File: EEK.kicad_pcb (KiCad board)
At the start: 2 copper layers, 165 x 51.8 mm, 52 parts, among them J1 Screw_Terminal_01x02

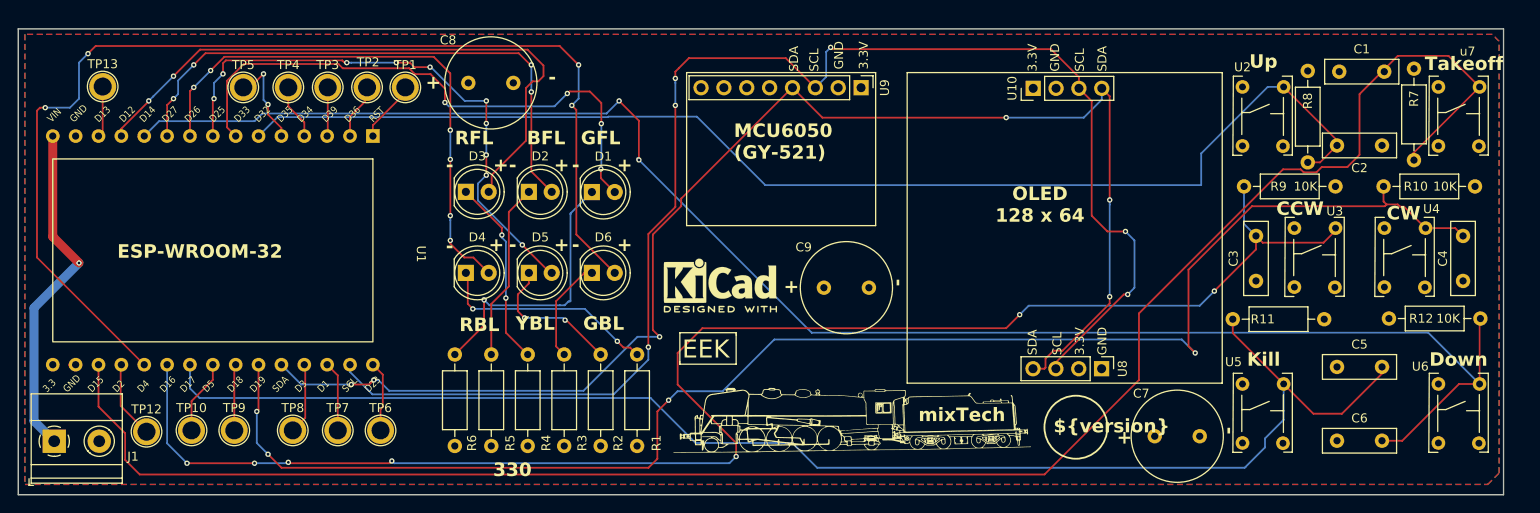
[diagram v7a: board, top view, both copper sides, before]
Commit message: Change footprint to SMD
Change footprint to SMD
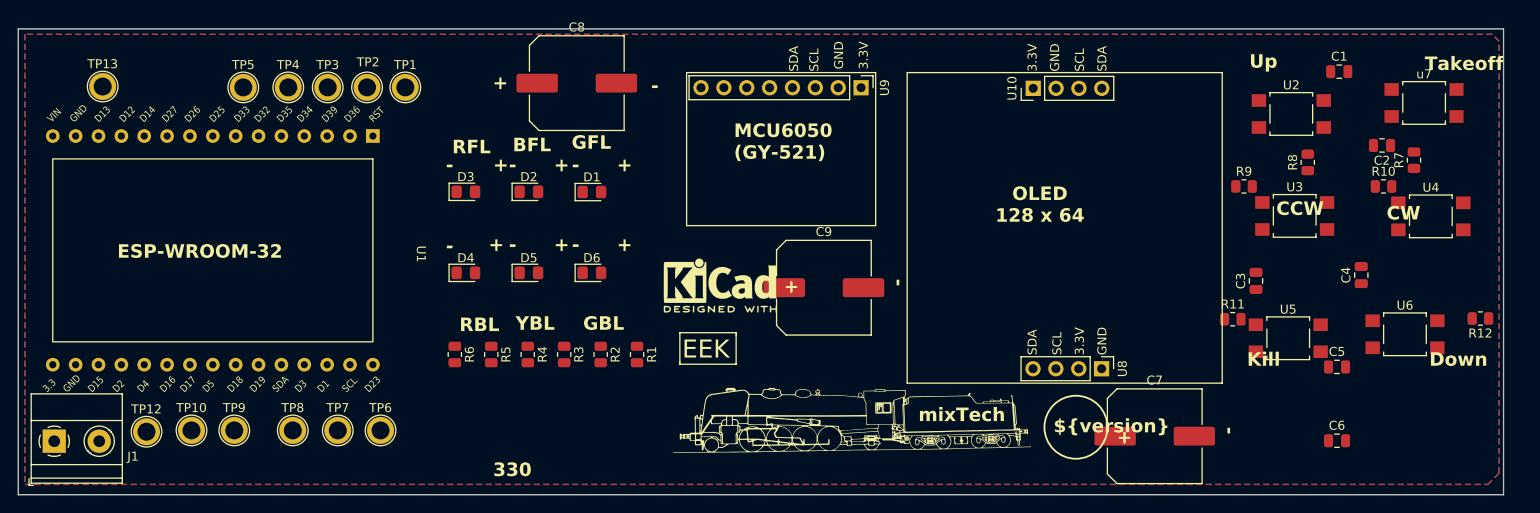
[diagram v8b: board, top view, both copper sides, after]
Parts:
- C1, C2, C3, C4, C5, C6: footprint Capacitor_THT:C_Disc_D8.0mm_W2.5mm_P5.00mm -> Capacitor_SMD:C_0805_2012Metric
- C7, C8, C9: footprint Capacitor_THT:C_Radial_D10.0mm_H12.5mm_P5.00mm -> Capacitor_SMD:C_Elec_10x10.2
- D1, D2, D3, D4, D5, D6: footprint LED_THT:LED_D5.0mm -> LED_SMD:LED_0805_2012Metric_Pad1.15x1.40mm_HandSolder
- R1, R10, R11, R12, R2, R3, R4, R5, R6, R7, R8, R9: footprint Resistor_THT:R_Axial_DIN0207_L6.3mm_D2.5mm_P10.16mm_Horizontal -> Resistor_SMD:R_0805_2012Metric
- U2, U3, U4, U5, U6, u7: footprint PH_lib:SW_Tactile -> Button_Switch_SMD:SW_SPST_TL3305A
- moved C8 12.1 mm to (104.5, 82.8)
- moved C4 11.3 mm to (191.7, 104.1)
- moved u7 9.57 mm to (198.7, 85.0)
- moved U6 8.81 mm to (196.6, 110.7)
- moved U2 8.09 mm to (183.9, 86.2)
- moved U3 6.27 mm to (184.3, 97.5)
- moved U4 3.78 mm to (199.4, 97.6)
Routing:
- net /Takeoff: track 203.4 -> 0.00 mm
- net /Down: track 186.3 -> 0.00 mm, vias 2 -> 0
- net /CCw: track 174.2 -> 0.00 mm, vias 7 -> 0
- net /CW: track 170.4 -> 0.00 mm, vias 4 -> 0
- net /SCL: track 161.5 -> 0.00 mm, vias 6 -> 0
- net /Kill: track 159.3 -> 0.00 mm
- net /SDA: track 154.7 -> 0.00 mm, vias 6 -> 0
- net /Up: track 137.5 -> 0.00 mm
- net /GBL: track 124.9 -> 0.00 mm, vias 4 -> 0
- net /RFL: track 69.0 -> 0.00 mm, vias 2 -> 0
- net /GFL: track 63.5 -> 0.00 mm, vias 4 -> 0
- net /YBR: track 62.8 -> 0.00 mm, vias 10 -> 0
- net /BFL: track 62.8 -> 0.00 mm, vias 4 -> 0
- net /RBR: track 60.8 -> 0.00 mm, vias 6 -> 0
- net Net-(J1-Pin_1): track 38.2 -> 0.00 mm, vias 1 -> 0
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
